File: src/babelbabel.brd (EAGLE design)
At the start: 41 x 75.5 mm, 144 parts, among them CON1 CON-4P-TABS-JST_GH-RA, CON10 CON-6P-SM06B, CON101 PINHEAD_1X04-2.54, CON102 PINHEAD_1X03-2.54, CON11 PINHEAD_1X04-2.54, CON12 PINHEAD_1X06-2.54, CON15 PINHEAD_1X04-2.54, CON16 CON-4P-TABS-JST_GH-RA, CON2 PINHEAD_1X04-2.54, CON3 PINHEAD_1X04-2.54, CON4 USB-AA-PTH, CON5 CON-4P-TABS-JST_GH-RA, CON6 CON-4P-TABS-JST_GH-RA, CON7 USB-1, IC101 STM32F373CBT6-LQFP48, IC102 STM32F373RCT6, IC103 AP2127-3.3, IC105 SN65HVD232D, IC108 TPD3S014DBVR-SOT23-6, IC13 STM32F103CBT7, IC14 74LVC2T45, IC15 74LVC2T45, IC16 74LVC2T45, IC17 74LVC2T45, IC3 AP2127-3.3, IC9 FE1.1S, J1 CONNECTION-SMD, J2 CONNECTION-SMD, Q102 IRLML0030, Q8 16MHz, Q9 DMG1023UV-7

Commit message: All doubtful issues resolved
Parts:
- Q9: value DMG1023UV-7 -> NTZD3152PT1G
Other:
- board text removed: "2. Find coupled MOSFETs alternatives for DCP 3. Check MCU alternative package"
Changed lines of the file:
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@@
 <?xml version="1.0" encoding="utf-8"?>
 <!DOCTYPE eagle SYSTEM "eagle.dtd">
-<eagle version="9.6.2">
+<eagle version="9.6.0">
 <drawing>
 <settings>
@@
 <setting verticaltext="up"/>
 </settings>
-<grid distance="0.1" unitdist="mm" unit="mm" style="lines" multiple="1" display="yes" altdistance="5" altunitdist="mil" altunit="mil"/>
+<grid distance="1" unitdist="mm" unit="mm" style="lines" multiple="1" display="yes" altdistance="5" altunitdist="mil" altunit="mil"/>
 <layers>
 <layer number="1" name="Top" color="4" fill="1" visible="yes" active="yes"/>
@@
 <layer number="13" name="Route13" color="21" fill="1" visible="no" active="no"/>
 <layer number="14" name="Route14" color="22" fill="1" visible="no" active="no"/>
-<layer number="15" name="Route15" color="23" fill="1" visible="yes" active="yes"/>
+<layer number="15" name="Route15" color="23" fill="1" visible="no" active="yes"/>
 <layer number="16" name="Bottom" color="1" fill="1" visible="no" active="yes"/>
 <layer number="17" name="Pads" color="2" fill="1" visible="yes" active="yes"/>
@@
 </layers>
 <board>
-<fusionsync huburn="a.cGVyc29uYWw6dWUyYWE4ZDY4" projecturn="a.cGVyc29uYWw6dWUyYWE4ZDY4IzIwMTgxMTAxMTU3ODkyNjgx" f3durn="urn:adsk.wipprod:dm.lineage:kGuPgqnzRmWLHCf0r-cvPw" pcbguid="" lastpulledtime="" lastsyncedchangeguid="" latestrevisionid="23f56a24-089a-4aa2-8d88-7c919b1d14c9" lastsyncedrevisionid="23f56a24-089a-4aa2-8d88-7c919b1d14c9" lastboardhashguid="ecd9556e-f591-69f8-ffd6-2b87c3ad0fb6" lastpushedtime="2020-12-24T16:12:39Z" linktopcb3d="true"/>
+<fusionsync huburn="a.cGVyc29uYWw6dWUyYWE4ZDY4" projecturn="a.cGVyc29uYWw6dWUyYWE4ZDY4IzIwMTgxMTAxMTU3ODkyNjgx" f3durn="urn:adsk.wipprod:dm.lineage:kGuPgqnzRmWLHCf0r-cvPw" pcbguid="" lastpulledtime="" lastsyncedchangeguid="" latestrevisionid="23f56a24-089a-4aa2-8d88-7c919b1d14c9" lastsyncedrevisionid="23f56a24-089a-4aa2-8d88-7c919b1d14c9" lastboardhashguid="ecd9556e-f591-69f8-ffd6-2b87c3ad0fb6" lastpushedtime="2020-12-24T16:12:39Z" linktopcb3d="%12"/>
 <plain>
 <wire x1="41" y1="33.75" x2="41" y2="32.35" width="0.01" layer="49"/>
@@
 <wire x1="32.9" y1="10.05" x2="33.9" y2="10.05" width="0.01" layer="110"/>
 <wire x1="33.4" y1="10.45" x2="33.4" y2="9.65" width="0.01" layer="110"/>
-<text x="44.8" y="24.8" size="1.778" layer="51">
-2. Find coupled MOSFETs alternatives for DCP
-3. Check MCU alternative package</text>
 <wire x1="41" y1="33" x2="40" y2="32" width="0.01" layer="20" curve="90"/>
 <wire x1="40" y1="32" x2="40" y2="18.5" width="0.01" layer="20"/>
@@
 <attribute name="TOLERANCE" value="1%" x="10.6" y="3" size="1.778" layer="27" rot="R180" display="off"/>
 </element>
-<element name="Q9" library="mosfet" library_urn="urn:adsk.eagle:library:2640523" package="SOT-563" package3d_urn="urn:adsk.eagle:package:8711362/3" value="DMG1023UV-7" x="26.825" y="16.075" smashed="yes">
-<attribute name="DIGIKEY#" value="DMG1023UV-7DICT-ND" x="26.825" y="16.075" size="1.778" layer="27" display="off"/>
-<attribute name="MANF" value="Diodes Incorporated" x="26.825" y="16.075" size="1.778" layer="27" display="off"/>
-<attribute name="MANF#" value="DMG1023UV-7" x="26.825" y="16.075" size="1.778" layer="27" display="off"/>
+<element name="Q9" library="mosfet" library_urn="urn:adsk.eagle:library:2640523" package="SOT-563" package3d_urn="urn:adsk.eagle:package:8711362/3" value="NTZD3152PT1G" x="26.825" y="16.075" smashed="yes">
+<attribute name="DIGIKEY#" value="NTZD3152PT1GOSCT-ND" x="26.825" y="16.075" size="1.778" layer="27" display="off"/>
+<attribute name="LCSC#" value="C393372" x="26.825" y="16.075" size="1.778" layer="27" display="off"/>
+<attribute name="MANF" value="ON Semiconductor" x="26.825" y="16.075" size="1.778" layer="27" display="off"/>
+<attribute name="MANF#" value="NTZD3152PT1G" x="26.825" y="16.075" size="1.778" layer="27" display="off"/>
 <attribute name="NAME" x="26.825" y="16.075" size="0.5" layer="25" font="vector" ratio="15" rot="R180" align="center"/>
 <attribute name="PACKAGE" value="SOT-563" x="26.825" y="16.075" size="1.778" layer="27" display="off"/>
@@
 </element>
 <element name="IC102" library="stm32" library_urn="urn:adsk.eagle:library:2473361" package="TQFP64" package3d_urn="urn:adsk.eagle:package:2473349/4" value="STM32F373RCT6" x="11.7" y="-25.45" smashed="yes" rot="R90">
-<attribute name="DIGIKEY#" value="" x="11.7" y="-25.45" size="1.778" layer="27" rot="R90" display="off"/>
+<attribute name="DIGIKEY#" value="497-13252-ND" x="11.7" y="-25.45" size="1.778" layer="27" rot="R90" display="off"/>
 <attribute name="LCSC#" value="C84174" x="11.7" y="-25.45" size="1.778" layer="27" rot="R90" display="off"/>
 <attribute name="MANF" value="STMicroelectronics" x="11.7" y="-25.45" size="1.778" layer="27" rot="R90" display="off"/>
@@
 </element>
 <element name="BABEL2:IC2" library="stm32" library_urn="urn:adsk.eagle:library:2473361" package="TQFP64" package3d_urn="urn:adsk.eagle:package:2473349/4" value="STM32F373RCT6" x="11.7" y="-7.45" smashed="yes" rot="R90">
-<attribute name="DIGIKEY#" value="" x="11.7" y="-7.45" size="1.778" layer="27" rot="R90" display="off"/>
+<attribute name="DIGIKEY#" value="497-13252-ND" x="11.7" y="-7.45" size="1.778" layer="27" rot="R90" display="off"/>
 <attribute name="LCSC#" value="C84174" x="11.7" y="-7.45" size="1.778" layer="27" rot="R90" display="off"/>
 <attribute name="MANF" value="STMicroelectronics" x="11.7" y="-7.45" size="1.778" layer="27" rot="R90" display="off"/>
@@
 <vertex x="35" y="-15.75"/>
 </polygon>
-<wire x1="35.64" y1="-27.325" x2="35.49644375" y2="-27.18144375" width="0.2" layer="1"/>
 <via x="35.19644375" y="-26.45355625" extent="1-16" drill="0.3" diameter="0.5"/>
 <via x="35.79644375" y="-26.45355625" extent="1-16" drill="0.3" diameter="0.5"/>
@@
 <vertex x="35" y="2.15"/>
 </polygon>
-<wire x1="35.64" y1="-9.325" x2="35.49644375" y2="-9.18144375" width="0.2" layer="1"/>
 <via x="35.19644375" y="-8.45355625" extent="1-16" drill="0.3" diameter="0.5"/>
 <via x="35.79644375" y="-8.45355625" extent="1-16" drill="0.3" diameter="0.5"/>

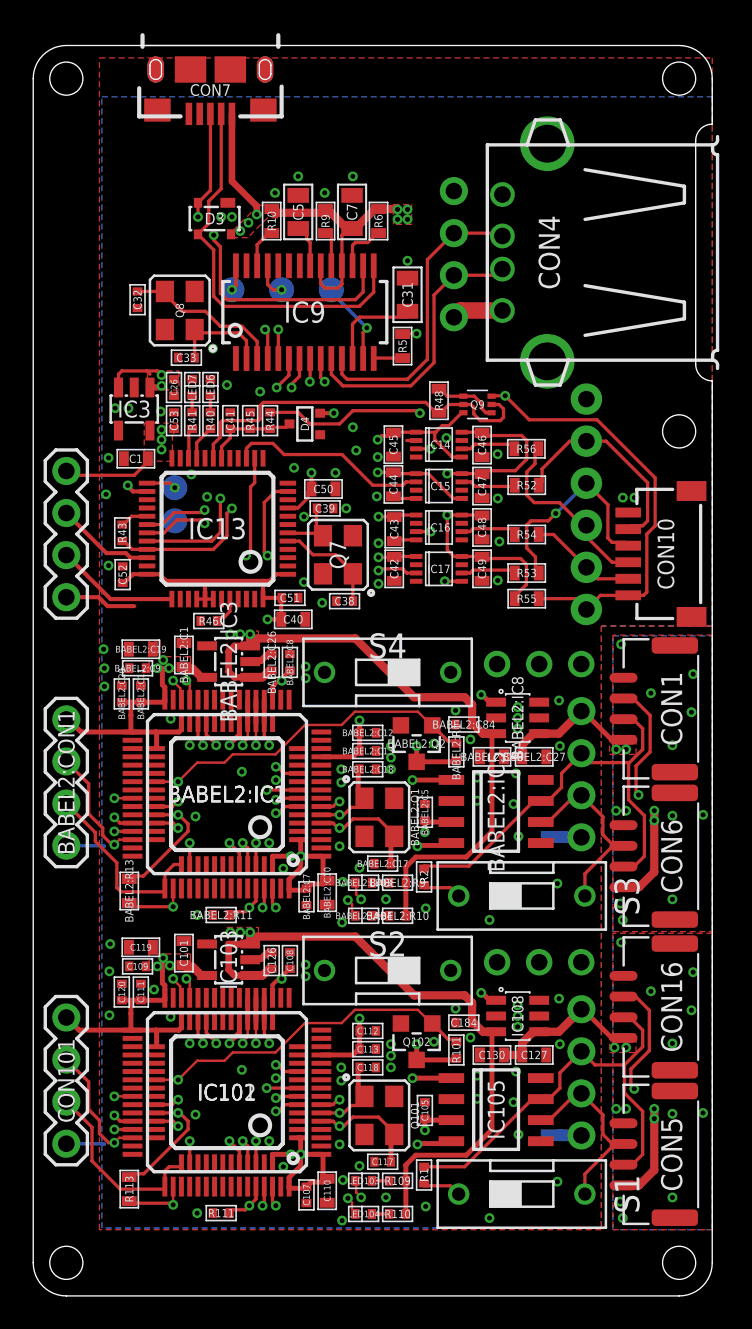
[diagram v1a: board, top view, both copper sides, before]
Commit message: CAN transciever replaced
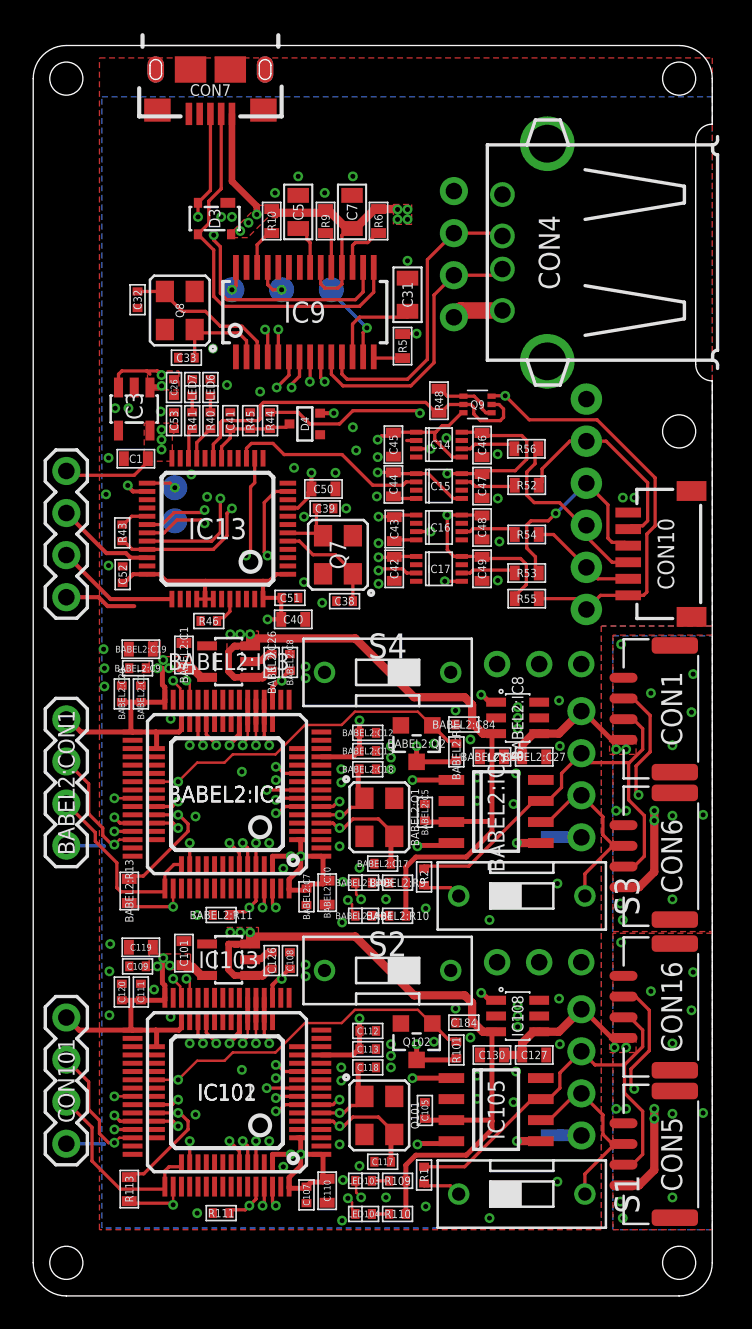
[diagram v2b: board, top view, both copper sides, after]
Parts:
- BABEL2:C17, BABEL2:C18, C117, C118: value 18pF -> 20pF
- BABEL2:IC5, IC105: value SN65HVD232D -> TJA1051-SO8
- BABEL2:Q1, Q101: value (none) -> 16MHz
- BABEL2:Q2, Q102: value IRLML0030 -> 2N7002
- Q7: value (none) -> 8MHz
- turned BABEL2:IC3 to 90 degrees
- turned D3 to 180 degrees
- turned IC103 to 90 degrees
- turned IC3 to 180 degrees
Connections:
- net BABEL1:VDD_3V3: now also IC105.5; no longer C105.2, IC105.3
- net BABEL2:VDD_3V3: now also BABEL2:IC5.5; no longer BABEL2:C5.2, BABEL2:IC5.3
- net GND: now also BABEL2:IC5.8, IC105.8
- net VDD_5V: now also BABEL2:C5.2, BABEL2:IC5.3, C105.2, IC105.3
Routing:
- net VDD_5V: track 173.1 -> 181.2 mm
- net BABEL2:VDD_3V3: track 87.8 -> 91.1 mm
- net BABEL1:VDD_3V3: track 88.0 -> 91.1 mm
- net GND: vias 117 -> 115

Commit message: Babel part attributes added
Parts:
- removed BABEL2:C19: 1µF, rc:C0603
- added C219: 1uF, rc:C0402
- C101, C110, C127, C130, C201, C210, C227, C230: value 4.7µF -> 4.7uF
- C105, C107, C108, C184, C205, C207, C208, C284: value 0.1µF -> 0.1uF
- C112, C120, C126, C212, C220, C226: value 1µF -> 1uF
- C119: value 1µF -> 1uF; device rc:C0603 -> rc:C0402
- moved LED6 1.30 mm to (12.0, 17.0), turned to 0 degrees
- moved LED7 0.41 mm to (10.0, 17.0), turned to 0 degrees
- moved C119 0.20 mm to (6.30, -16.7)
- renumbered BABEL2:C1 to C201, BABEL2:C10 to C210, BABEL2:C11 to C211, BABEL2:C12 to C212, BABEL2:C13 to C213, BABEL2:C17 to C217, BABEL2:C18 to C218, BABEL2:C20 to C220, BABEL2:C26 to C226, BABEL2:C27 to C227, BABEL2:C30 to C230, BABEL2:C5 to C205, BABEL2:C7 to C207, BABEL2:C8 to C208, BABEL2:C84 to C284, BABEL2:C9 to C209, BABEL2:CON1 to CON201, BABEL2:CON2 to CON202, BABEL2:IC1 to IC201, BABEL2:IC2 to IC202, BABEL2:IC3 to IC203, BABEL2:IC5 to IC205, BABEL2:IC8 to IC208, BABEL2:LED3 to LED203, BABEL2:LED4 to LED204, BABEL2:Q1 to Q201, BABEL2:Q2 to Q202, BABEL2:R1 to R201, BABEL2:R10 to R210, BABEL2:R11 to R211, BABEL2:R13 to R213, BABEL2:R9 to R209
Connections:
- net BABEL2:VDD_3V3: now also C219.2; no longer BABEL2:C19.2
- net GND: now also C219.1; no longer BABEL2:C19.1
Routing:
- net N$39: track 1.00 -> 1.73 mm
- net GND: vias 115 -> 123

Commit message: Massive attribute update
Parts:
- C1, C40, C50: value 4.7µF -> 4.7uF
- C26: value 1µF -> 1uF
- C32, C33: value 18pF -> 20pF
- C38, C39: value 18pF -> 10pF
- C41, C51, C52, C53: value 0.1µF -> 0.1uF
- C42, C43, C44, C45, C46, C47, C48, C49: value 0.1µF -> 0.1uF; device C_digikey:C0603 -> rc:C0402
- R1, R2: value 100K -> 120R; device rc:R0402 -> rc:R0603
- R48, R54, R56: device R_digikey:R0603 -> rc:R0402
- R52, R53, R55: device R_digikey:R0603 -> rc:R0603
- moved R1 0.25 mm to (23.6, -30.7)
- moved R2 0.20 mm to (23.6, -12.7)
- moved R109 0.05 mm to (21.9, -30.8)
- moved R110 0.05 mm to (21.9, -32.8)
- moved R209 0.05 mm to (21.9, -12.8)
- moved R210 0.05 mm to (21.9, -14.8)
- turned D3 to 270 degrees
- turned IC103 to 0 degrees
- turned IC203 to 0 degrees
- turned IC3 to 90 degrees
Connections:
- net CONSOLE_RX: now also R56.2; no longer R56.P$2
- net CONSOLE_TX: now also R54.2; no longer R54.P$2
- net GND: now also C42.2, C43.2, C44.2, C45.2, C46.1, C47.1, C48.1, C49.1; no longer C42.P$2, C43.P$2, C44.P$2, C45.P$2, C46.P$1, C47.P$1, C48.P$1, C49.P$1
- net N$44: now also R48.1; no longer R48.P$1
- net PWR_BR: now also R48.2; no longer R48.P$2
- net TCK: now also R52.2; no longer R52.P$2
- net TMS: now also R53.2; no longer R53.P$2
- net TPWR: now also R55.2; no longer R55.P$2
- net VDD_3V3: now also C42.1, C43.1, C44.1, C45.1; no longer C42.P$1, C43.P$1, C44.P$1, C45.P$1
- net XRXD: now also R54.1; no longer R54.P$1
- net XTCK: now also R52.1; no longer R52.P$1
- net XTMS: now also R53.1; no longer R53.P$1
- net XTPWR: now also C46.2, C47.2, C48.2, C49.2, R55.1; no longer C46.P$2, C47.P$2, C48.P$2, C49.P$2, R55.P$1
- net XTXD: now also R56.1; no longer R56.P$1
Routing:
- net GND: track 17.9 -> 13.8 mm
- net VDD_3V3: track 82.1 -> 82.6 mm

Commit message: BOM improvement
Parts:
- D4: value BAT30SWFILM -> BAT54SWT1G
- Q8: value 16MHz -> 12MHz
- R54, R56: device rc:R0402 -> rc:R0603

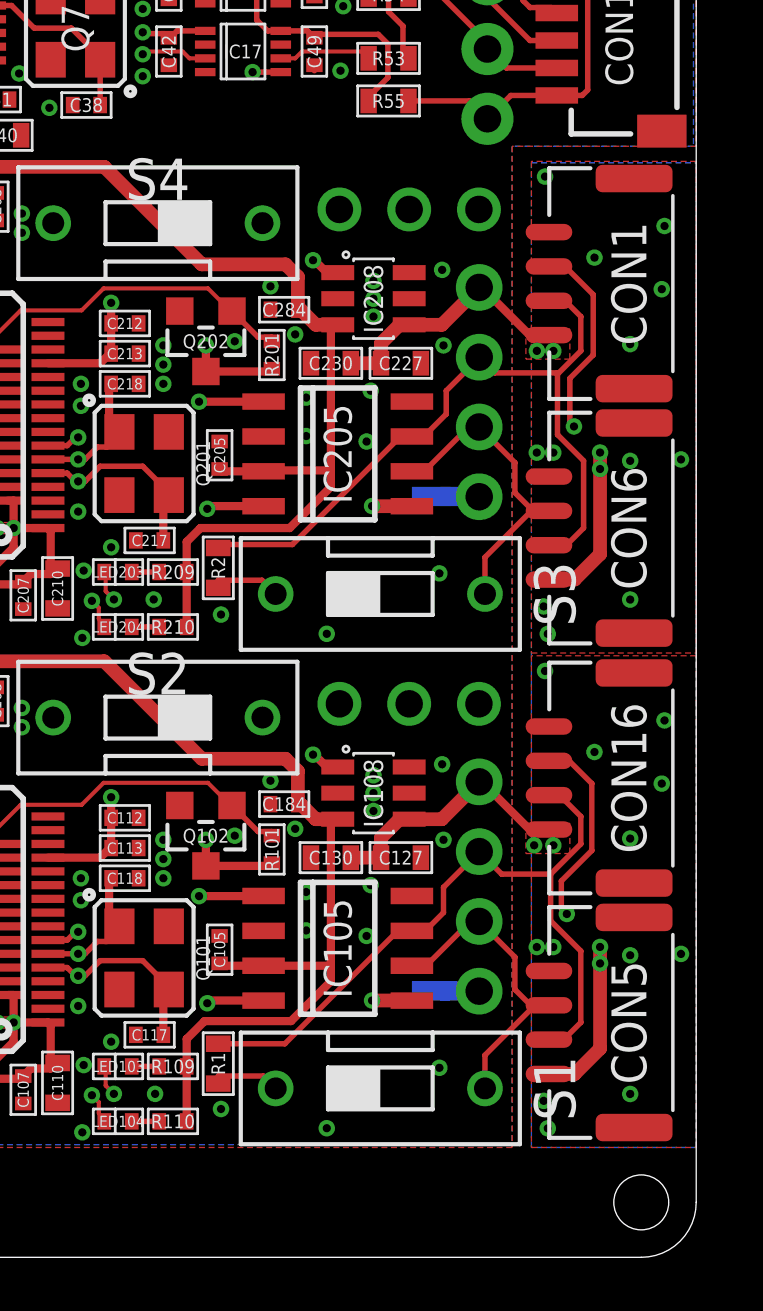
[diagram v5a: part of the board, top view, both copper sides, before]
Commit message: UAVCAN PLS connectors fixed
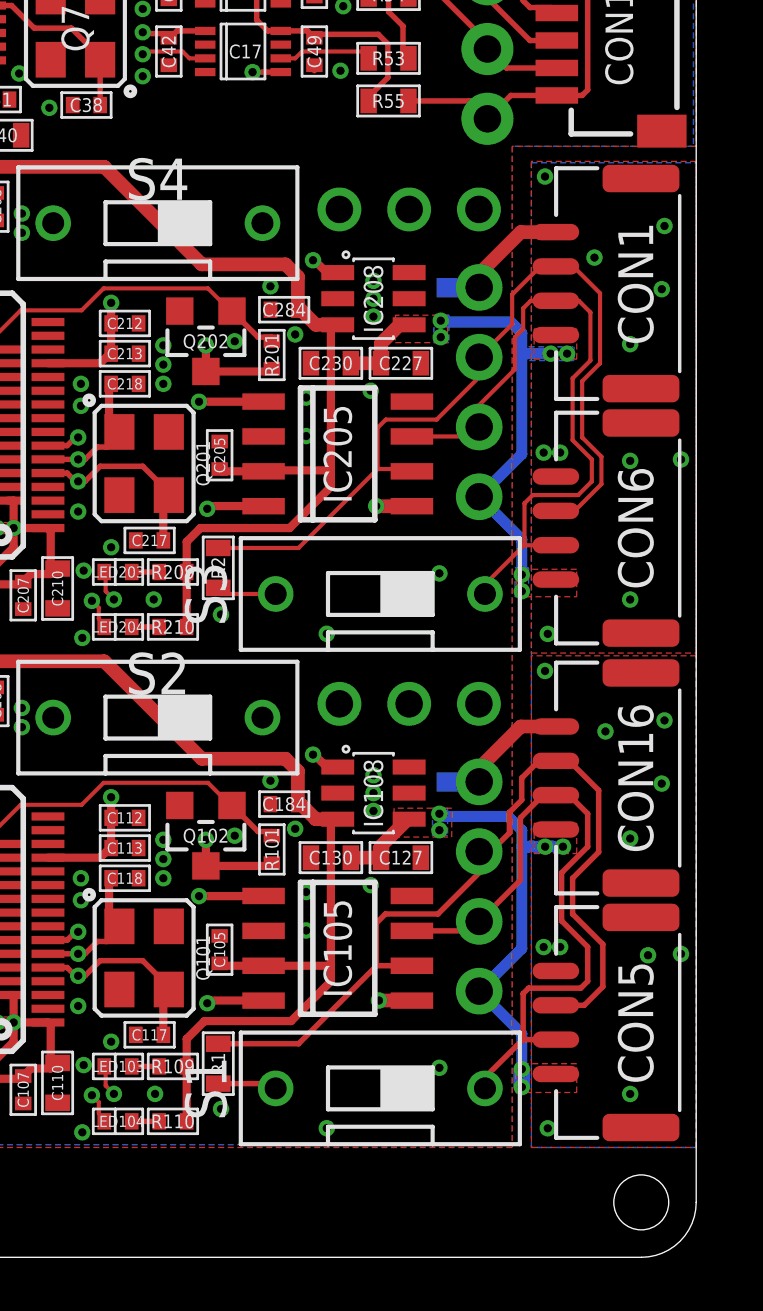
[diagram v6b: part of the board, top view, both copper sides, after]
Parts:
- moved J1 7.65 mm to (32.2, -20.4)
- moved J2 7.65 mm to (32.2, -2.45)
- moved CON1 0.25 mm to (38.8, -2.30)
- moved CON16 0.25 mm to (38.8, -20.3)
- moved CON5 0.25 mm to (38.8, -29.2)
- moved CON6 0.25 mm to (38.8, -11.2)
- turned CON2 to 90 degrees
- turned CON3 to 90 degrees
- turned S1 to 90 degrees
- turned S3 to 90 degrees
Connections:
- removed net CANH2: CON1.2, CON2.2, CON6.2, IC205.7, R2.2
- removed net N$4: R1.1, S1.1
- new net N$1: R1.1, S1.10
- new net N$2: R2.1, S3.10
- net CANH1: now also S1.1; no longer R1.2
- net CANL1: now also R1.2; no longer S1.10
- net CANL2: now also R2.2; no longer S3.10
- net N$6: now also CON1.2, CON2.2, CON6.2, IC205.7; no longer R2.1
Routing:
- net CANH2: track 27.5 -> 0.00 mm
- net N$6: track 2.57 -> 24.9 mm
- net CANL1: track 22.4 -> 32.1 mm, vias 1 -> 0
- net CANL2: track 22.1 -> 31.3 mm, vias 1 -> 0
- net CAN1_VDD1: track 21.0 -> 17.4 mm, vias 4 -> 6
- net CAN1_VDD: track 21.1 -> 18.3 mm, vias 4 -> 6
- net N$4: track 2.55 -> 0.00 mm
- net CANH1: track 27.2 -> 24.7 mm
- net N$2: track 0.00 -> 2.18 mm
- net N$1: track 0.00 -> 2.16 mm
- net GNDD: track 7.83 -> 8.84 mm, vias 24 -> 22
- net GND: vias 123 -> 117
- added copper zone on layer 16, net CAN1_VDD
- added copper zone on layer 16, net CAN1_VDD1
